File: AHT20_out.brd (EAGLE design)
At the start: 25.4 x 17.8 mm, 19 parts, among them U1 AHT20

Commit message: Output embedded in .brd as lib, vital to handling anchor points!
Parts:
- added pLabel0: (no value), pinguin:pLabel0
- added pLabel1: (no value), pinguin:pLabel1
- added pLabel2: (no value), pinguin:pLabel2

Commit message: Heck yeah, anchor starting to work
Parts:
- turned pLabel1 to 12 degrees
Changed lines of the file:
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@@
         <text align="center" font="vector" layer="21" ratio="14" size="1.016" x="14.097" y="0.889">SCL</text>
         <text align="center" font="vector" layer="21" ratio="14" size="1.016" x="16.637" y="4.191">SDA</text>
-        <text align="center" layer="172" ratio="15" size="1.778" x="12.7" y="16.51">AHT20</text>
+        <text align="center" layer="172" ratio="15" rot="R12" size="1.778" x="12.7" y="16.51">AHT20</text>
         <text align="center" layer="172" ratio="15" size="1.143" x="14.351" y="14.605">Temp &amp; Humidity</text>
         <dimension dtype="vertical" layer="47" textsize="1.778" unit="inch" x1="12.7" x2="12.7" x3="29.337" y1="2.54" y2="15.24" y3="8.89"/>
@@
         </element>
         <element library="pinguin" name="pLabel0" package="pLabel0" rot="R0" smashed="yes" x="11.43" y="4.191"/>
-        <element library="pinguin" name="pLabel1" package="pLabel1" rot="R0" smashed="yes" x="12.7" y="16.51"/>
+        <element library="pinguin" name="pLabel1" package="pLabel1" rot="R12" smashed="yes" x="12.7" y="16.51"/>
         <element library="pinguin" name="pLabel2" package="pLabel2" rot="R0" smashed="yes" x="14.351" y="14.605"/>
       </elements>

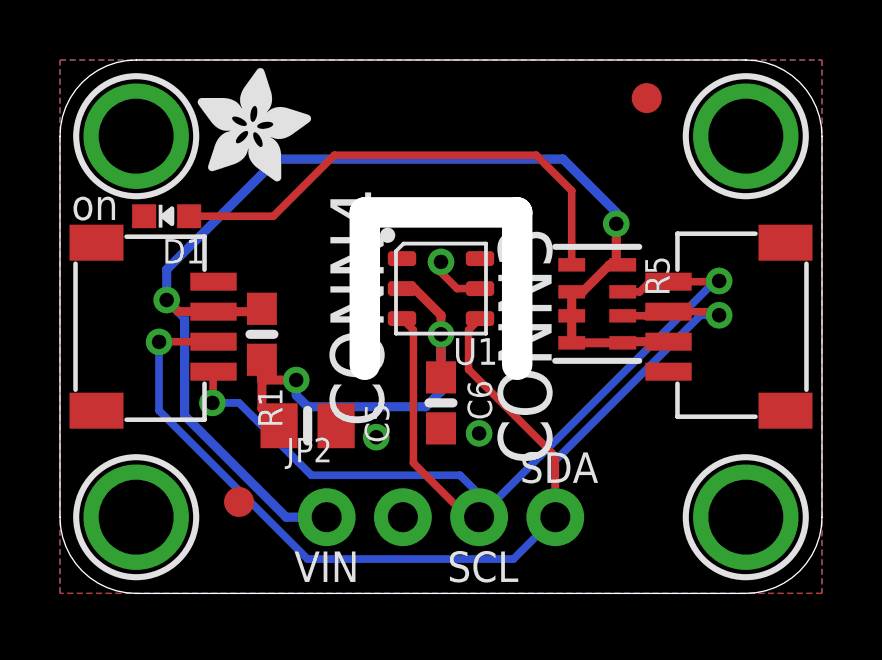
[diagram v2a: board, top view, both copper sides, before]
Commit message: Starting to handle text alignment, monospace font
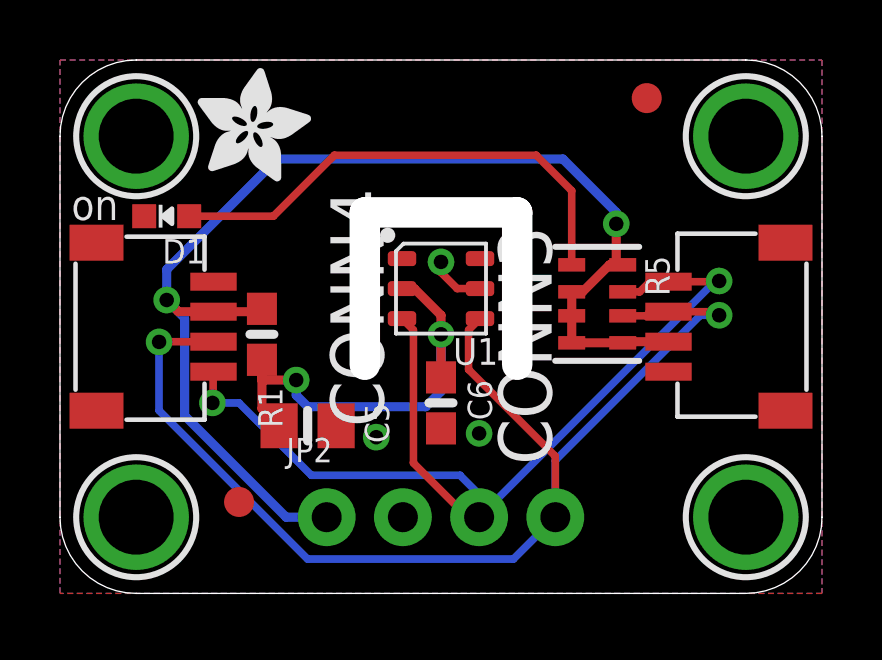
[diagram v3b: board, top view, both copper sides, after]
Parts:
- added pLabel10: (no value), pinguin:pLabel10
- added pLabel11: (no value), pinguin:pLabel11
- added pLabel12: (no value), pinguin:pLabel12
- added pLabel13: (no value), pinguin:pLabel13
- added pLabel14: (no value), pinguin:pLabel14
- added pLabel3: (no value), pinguin:pLabel3
- added pLabel4: (no value), pinguin:pLabel4
- added pLabel5: (no value), pinguin:pLabel5
- added pLabel6: (no value), pinguin:pLabel6
- added pLabel7: (no value), pinguin:pLabel7
- added pLabel8: (no value), pinguin:pLabel8
- added pLabel9: (no value), pinguin:pLabel9
- moved pLabel2 13.7 mm to (14.1, 0.89)
- moved pLabel1 12.4 mm to (11.4, 4.19), turned to 0 degrees
- moved pLabel0 4.17 mm to (8.89, 0.89)
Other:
- board text added: "Hello"
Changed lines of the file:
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@@
         <wire layer="20" width="0" x1="22.86" x2="2.54" y1="17.78" y2="17.78"/>
         <wire curve="90" layer="20" width="0" x1="2.54" x2="0" y1="17.78" y2="15.24"/>
-        <text align="center" font="vector" layer="21" ratio="14" size="1.016" x="8.89" y="0.889">VIN</text>
+        <text align="center" font="fixed" layer="172" ratio="14" size="1.016" x="8.89" y="0.889">VIN</text>
         <text align="center" font="vector" layer="172" ratio="14" size="1.016" x="11.43" y="4.191">GND</text>
-        <text align="center" font="vector" layer="21" ratio="14" size="1.016" x="14.097" y="0.889">SCL</text>
-        <text align="center" font="vector" layer="21" ratio="14" size="1.016" x="16.637" y="4.191">SDA</text>
+        <text align="center" font="fixed" layer="172" ratio="14" size="1.016" x="14.097" y="0.889">SCL</text>
+        <text align="center" font="fixed" layer="172" ratio="14" size="1.016" x="16.637" y="4.191">SDA</text>
         <text align="center" layer="172" ratio="15" rot="R12" size="1.778" x="12.7" y="16.51">AHT20</text>
         <text align="center" layer="172" ratio="15" size="1.143" x="14.351" y="14.605">Temp &amp; Humidity</text>
@@
 addr
 0x38</text>
+        <text align="center" layer="172" ratio="15" rot="R15" size="0.508" x="7.747" y="11.303">Hello</text>
+        <text align="bottom-center" layer="172" ratio="15" rot="R353" size="0.508" x="7.747" y="11.811">Hello</text>
+        <text align="top-center" layer="172" ratio="15" rot="R352" size="0.508" x="7.747" y="10.795">Hello</text>
+        <text align="center-right" layer="172" ratio="15" rot="R355" size="0.508" x="6.731" y="11.303">Hello</text>
+        <text align="bottom-right" layer="172" ratio="15" rot="R3" size="0.508" x="6.731" y="11.811">Hello</text>
+        <text align="top-right" layer="172" ratio="15" rot="R31" size="0.508" x="6.731" y="10.795">Hello</text>
+        <text align="center-left" layer="172" ratio="15" rot="R357" size="0.508" x="8.763" y="11.303">Hello</text>
+        <text layer="172" ratio="15" rot="R22" size="0.508" x="8.763" y="11.811">Hello</text>
+        <text align="top-left" layer="172" ratio="15" rot="R338" size="0.508" x="8.763" y="10.795">Hello</text>
       </plain>
       <attributes>
@@
           <attribute font="vector" layer="27" name="VALUE" ratio="10" rot="R270" size="1.016" x="7.874" y="10.033"/>
         </element>
-        <element library="pinguin" name="pLabel0" package="pLabel0" rot="R0" smashed="yes" x="11.43" y="4.191"/>
-        <element library="pinguin" name="pLabel1" package="pLabel1" rot="R12" smashed="yes" x="12.7" y="16.51"/>
-        <element library="pinguin" name="pLabel2" package="pLabel2" rot="R0" smashed="yes" x="14.351" y="14.605"/>
+        <element library="pinguin" name="pLabel0" package="pLabel0" rot="R0" smashed="yes" x="8.89" y="0.889"/>
+        <element library="pinguin" name="pLabel1" package="pLabel1" rot="R0" smashed="yes" x="11.43" y="4.191"/>
+        <element library="pinguin" name="pLabel2" package="pLabel2" rot="R0" smashed="yes" x="14.097" y="0.889"/>
+        <element library="pinguin" name="pLabel3" package="pLabel3" rot="R0" smashed="yes" x="16.637" y="4.191"/>
+        <element library="pinguin" name="pLabel4" package="pLabel4" rot="R12" smashed="yes" x="12.7" y="16.51"/>
+        <element library="pinguin" name="pLabel5" package="pLabel5" rot="R0" smashed="yes" x="14.351" y="14.605"/>
+        <element library="pinguin" name="pLabel6" package="pLabel6" rot="R15" smashed="yes" x="7.747" y="11.303"/>
+        <element library="pinguin" name="pLabel7" package="pLabel7" rot="R353" smashed="yes" x="7.747" y="11.811"/>
+        <element library="pinguin" name="pLabel8" package="pLabel8" rot="R352" smashed="yes" x="7.747" y="10.795"/>
+        <element library="pinguin" name="pLabel9" package="pLabel9" rot="R355" smashed="yes" x="6.731" y="11.303"/>
+        <element library="pinguin" name="pLabel10" package="pLabel10" rot="R3" smashed="yes" x="6.731" y="11.811"/>
+        <element library="pinguin" name="pLabel11" package="pLabel11" rot="R31" smashed="yes" x="6.731" y="10.795"/>
+        <element library="pinguin" name="pLabel12" package="pLabel12" rot="R357" smashed="yes" x="8.763" y="11.303"/>
+        <element library="pinguin" name="pLabel13" package="pLabel13" rot="R22" smashed="yes" x="8.763" y="11.811"/>
+        <element library="pinguin" name="pLabel14" package="pLabel14" rot="R338" smashed="yes" x="8.763" y="10.795"/>
       </elements>
       <signals>
